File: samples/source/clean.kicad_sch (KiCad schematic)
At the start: 14 parts, among them J1 USB_5V_INPUT, U1 ESP32-WROOM-32E, U2 Waveshare_0.91_OLED, U3 TLV1117LV33

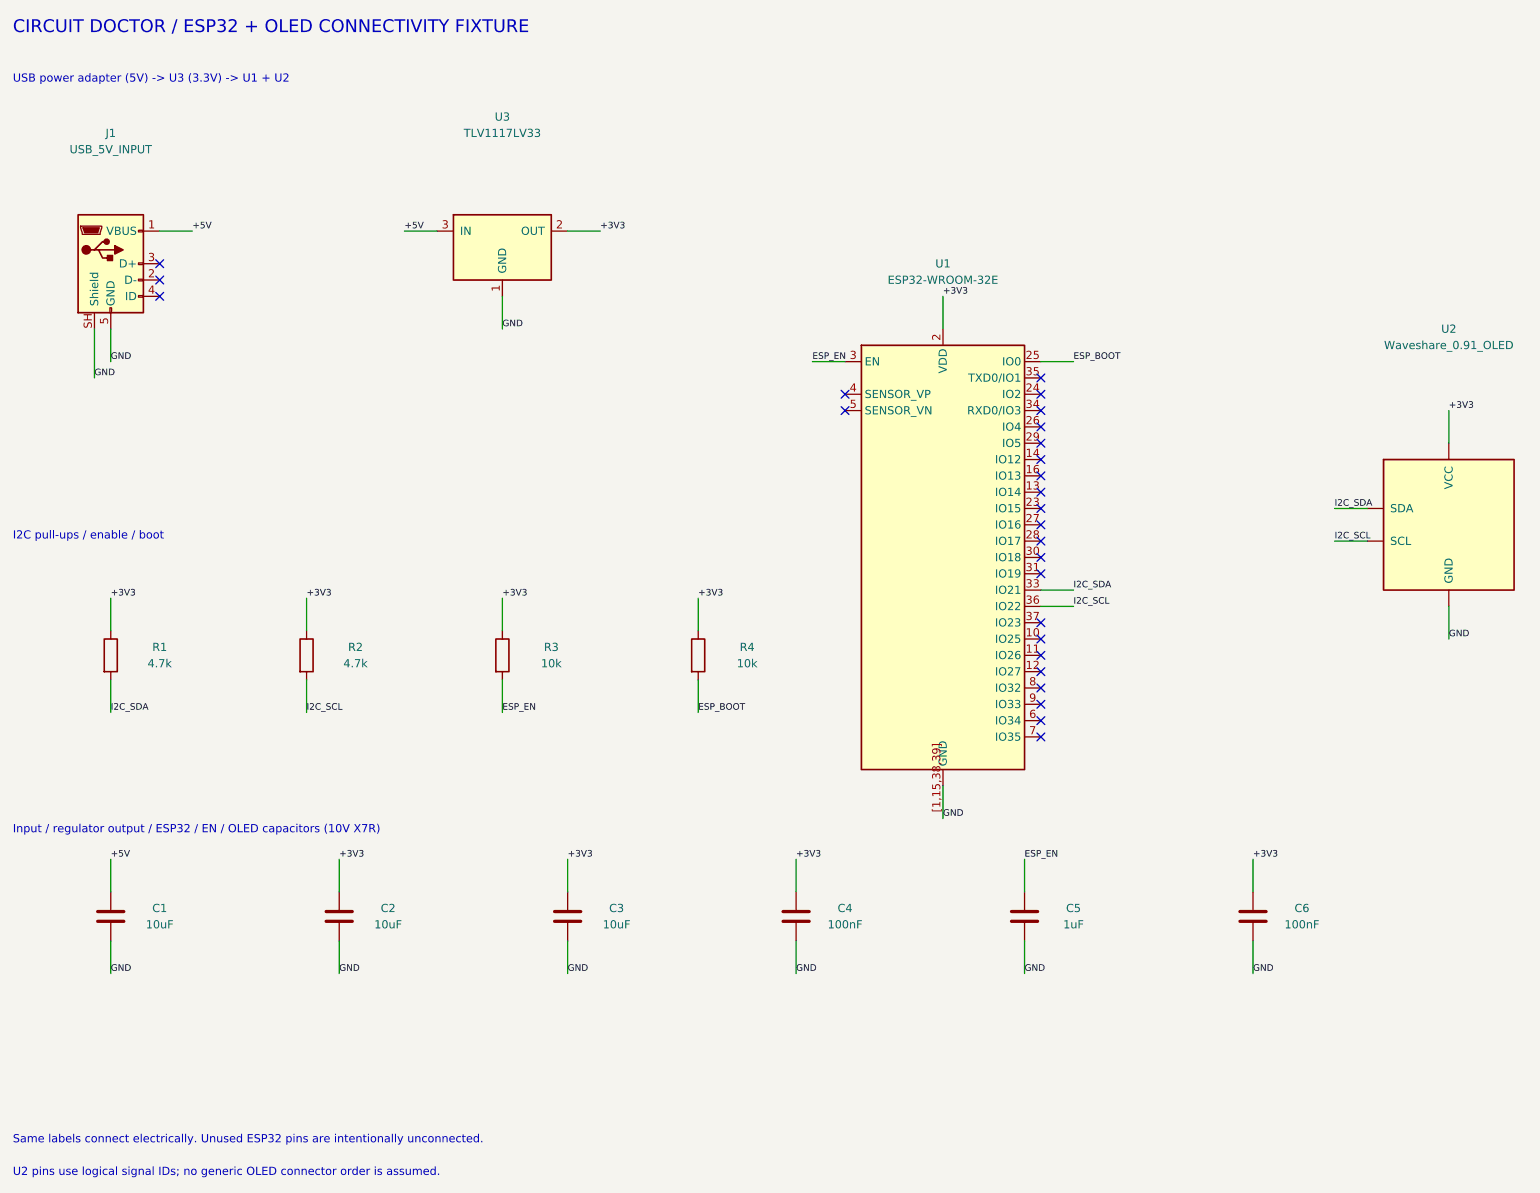
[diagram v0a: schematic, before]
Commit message: fix: use original Arduino LED samples with missing ground fault
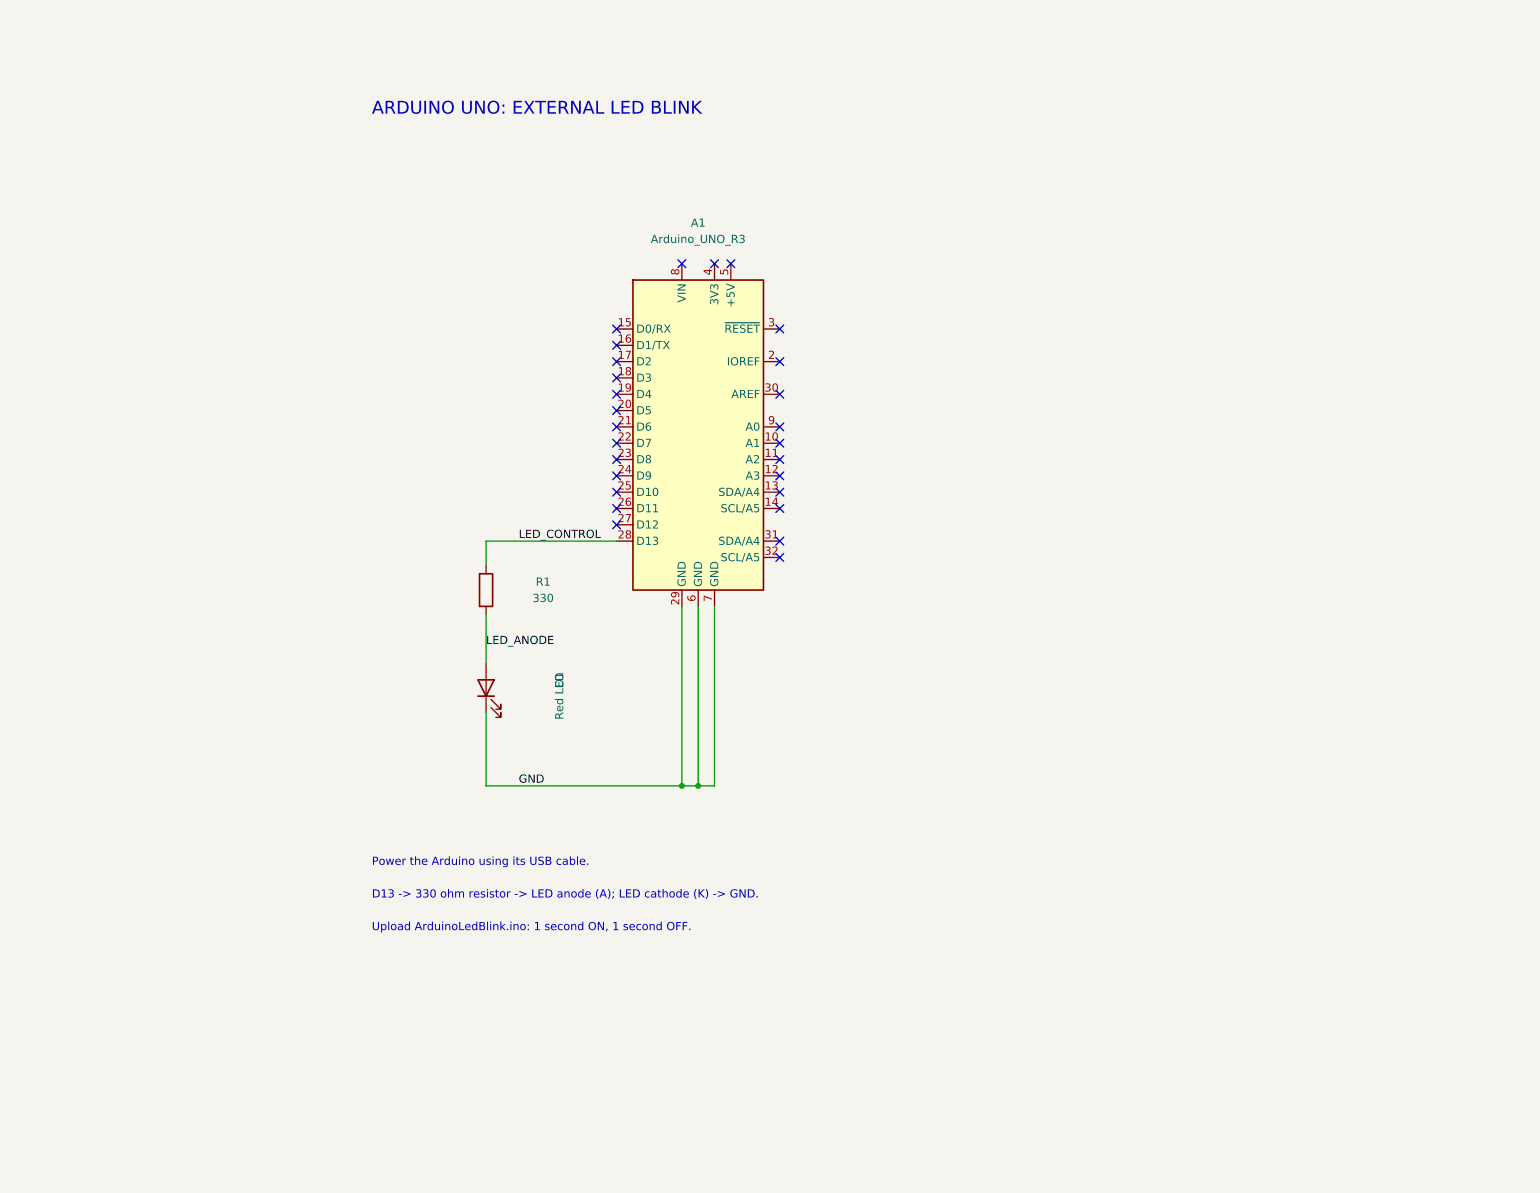
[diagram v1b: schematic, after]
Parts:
- removed C1, C2, C3: 10uF, symbol Device:C
- removed C4, C6: 100nF, symbol Device:C
- removed C5: 1uF, symbol Device:C
- removed J1: USB_5V_INPUT, symbol Connector:USB_B_Micro
- removed R2: 4.7k, symbol Device:R
- removed R3, R4: 10k, symbol Device:R
- removed U1: ESP32-WROOM-32E, symbol RF_Module:ESP32-WROOM-32E
- removed U2: Waveshare_0.91_OLED, symbol CircuitDoctor:Waveshare_0.91_OLED
- removed U3: TLV1117LV33, symbol CircuitDoctor:TLV1117LV33
- added A1: Arduino_UNO_R3, Module:Arduino_UNO_R3, symbol MCU_Module:Arduino_UNO_R3
- added D1: Red LED, LED_THT:LED_D5.0mm, symbol Device:LED
- R1: value 4.7k -> 330; footprint (none) -> Resistor_THT:R_Axial_DIN0207_L6.3mm_D2.5mm_P7.62mm_Horizontal
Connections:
- net GND: now also A1.29 (GND), A1.6 (GND), A1.7 (GND), D1.1 (K)
- net +3V3 renamed LED_CONTROL
- net LED_CONTROL: now also A1.28 (D13)
- net I2C_SDA renamed LED_ANODE
- net LED_ANODE: now also D1.2 (A)
- no-connect marks 26 -> 27
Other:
- note added: "ARDUINO UNO: EXTERNAL LED BLINK"
- note added: "D13 -> 330 ohm resistor -> LED anode (A); LED cathode (K) -> GND."
- note added: "Power the Arduino using its USB cable."
- note added: "Upload ArduinoLedBlink.ino: 1 second ON, 1 second OFF."
- note removed: "CIRCUIT DOCTOR / ESP32 + OLED CONNECTIVITY FIXTURE"
- note removed: "I2C pull-ups / enable / boot"
- note removed: "Input / regulator output / ESP32 / EN / OLED capacitors (10V X7R)"
- note removed: "Same labels connect electrically. Unused ESP32 pins are intentionally unconnected."
- note removed: "U2 pins use logical signal IDs; no generic OLED connector order is assumed."
- note removed: "USB power adapter (5V) -> U3 (3.3V) -> U1 + U2"
- title: CircuitDoctor: ESP32 + I2C OLED -> Arduino Uno - External LED Blink
